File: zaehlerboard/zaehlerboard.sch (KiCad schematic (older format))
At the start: 10 parts, among them Q1 Q_Photo_NPN, U1 ESP1, U2 MCP1700-3.3, U3 LM293

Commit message: pin associations
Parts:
- C1: footprint Capacitor_THT:CP_Radial_D8.0mm_P5.00mm -> Capacitor_THT:C_Disc_D5.0mm_W2.5mm_P5.00mm
- R1, R2, R3: footprint (none) -> Resistor_THT:R_Axial_DIN0204_L3.6mm_D1.6mm_P7.62mm_Horizontal
- RV1: footprint (none) -> Potentiometer_THT:Potentiometer_ACP_CA9-V10_Vertical
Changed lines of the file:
@@
 F 0 "R2" H 5820 3396 50  0000 L CNN
 F 1 "22k" H 5820 3305 50  0000 L CNN
-F 2 "" V 5680 3350 50  0001 C CNN
+F 2 "Resistor_THT:R_Axial_DIN0204_L3.6mm_D1.6mm_P7.62mm_Horizontal" V 5680 3350 50  0001 C CNN
 F 3 "~" H 5750 3350 50  0001 C CNN
 	1    5750 3350
@@
 F 0 "R1" H 4630 3304 50  0000 R CNN
 F 1 "43" H 4630 3395 50  0000 R CNN
-F 2 "" V 4630 3350 50  0001 C CNN
+F 2 "Resistor_THT:R_Axial_DIN0204_L3.6mm_D1.6mm_P7.62mm_Horizontal" V 4630 3350 50  0001 C CNN
 F 3 "~" H 4700 3350 50  0001 C CNN
 	1    4700 3350
@@
 F 0 "RV1" V 6793 2550 50  0000 C CNN
 F 1 "10k" V 6884 2550 50  0000 C CNN
-F 2 "" H 7000 2550 50  0001 C CNN
+F 2 "Potentiometer_THT:Potentiometer_ACP_CA9-V10_Vertical" H 7000 2550 50  0001 C CNN
 F 3 "~" H 7000 2550 50  0001 C CNN
 	1    7000 2550
@@
 F 0 "C1" H 8465 3296 50  0000 L CNN
 F 1 "100nF" H 8465 3205 50  0000 L CNN
-F 2 "Capacitor_THT:CP_Radial_D8.0mm_P5.00mm" H 8388 3100 50  0001 C CNN
+F 2 "Capacitor_THT:C_Disc_D5.0mm_W2.5mm_P5.00mm" H 8388 3100 50  0001 C CNN
 F 3 "~" H 8350 3250 50  0001 C CNN
 	1    8350 3250
@@
 F 0 "R3" V 9843 1150 50  0000 C CNN
 F 1 "3k3" V 9934 1150 50  0000 C CNN
-F 2 "" V 9980 1150 50  0001 C CNN
+F 2 "Resistor_THT:R_Axial_DIN0204_L3.6mm_D1.6mm_P7.62mm_Horizontal" V 9980 1150 50  0001 C CNN
 F 3 "~" H 10050 1150 50  0001 C CNN
 	1    10050 1150

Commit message: update circuit
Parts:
- added J1: Screw_Terminal_01x02, TerminalBlock:TerminalBlock_Altech_AK300-2_P5.00mm, symbol Connector:Screw_Terminal_01x02
- RV1: footprint Potentiometer_THT:Potentiometer_ACP_CA9-V10_Vertical -> Potentiometer_THT:Potentiometer_ACP_CA9-H5_Horizontal
- U3: footprint Package_DIP:DIP-8_W10.16mm -> Package_DIP:DIP-8_W7.62mm_Socket
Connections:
- net GND: now also J1.1 (Pin_1)
- net VCC: now also J1.2 (Pin_2)
- net VDD: now also D1.2 (A); no longer D1.1 (K)
- net at R1.2: now also D1.1 (K); no longer D1.2 (A)
- no-connect marks 1 -> 0
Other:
- moved on the sheet: D1, U2, U3C
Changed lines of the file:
@@
 F 3 "~" H 4700 2650 50  0001 C CNN
 	1    4700 2650
-	0    1    1    0
+	0    -1   -1   0
 $EndComp
 $Comp
@@
 F 0 "U3" H 7450 2683 50  0000 C CNN
 F 1 "LM293" H 7450 2774 50  0000 C CNN
-F 2 "Package_DIP:DIP-8_W10.16mm" H 7400 3150 50  0001 C CNN
+F 2 "Package_DIP:DIP-8_W7.62mm_Socket" H 7400 3150 50  0001 C CNN
 F 3 "http://www.ti.com/lit/ds/symlink/tl081.pdf" H 7500 3250 50  0001 C CNN
 	1    7450 3050
@@
 	1    0    0    -1
 $EndComp
-$Comp
-L power:GND #PWR0105
-U 1 1 5D3768AA
-P 7650 2550
-F 0 "#PWR0105" H 7650 2300 50  0001 C CNN
-F 1 "GND" V 7655 2422 50  0000 R CNN
-F 2 "" H 7650 2550 50  0001 C CNN
-F 3 "" H 7650 2550 50  0001 C CNN
-	1    7650 2550
-	0    -1   -1   0
-$EndComp
 Wire Wire Line
 	6450 2550 6450 2400
@@
 L Regulator_Linear:MCP1700-3302E_TO92 U2
 U 1 1 5D3977D9
-P 3700 2050
-F 0 "U2" H 3700 1800 50  0000 C CNN
-F 1 "MCP1700-3.3" H 3700 1900 50  0000 C CNN
-F 2 "Package_TO_SOT_THT:TO-92" H 3700 2300 50  0001 C CIN
-F 3 "http://www.ti.com/lit/ds/symlink/lm1085.pdf" H 3700 2050 50  0001 C CNN
-	1    3700 2050
+P 3500 2500
+F 0 "U2" H 3500 2250 50  0000 C CNN
+F 1 "MCP1700-3.3" H 3500 2350 50  0000 C CNN
+F 2 "Package_TO_SOT_THT:TO-92" H 3500 2750 50  0001 C CIN
+F 3 "http://www.ti.com/lit/ds/symlink/lm1085.pdf" H 3500 2500 50  0001 C CNN
+	1    3500 2500
 	-1   0    0    1
 $EndComp
@@
 L power:GND #PWR02
 U 1 1 5D39ABD9
-P 3700 2900
-F 0 "#PWR02" H 3700 2650 50  0001 C CNN
-F 1 "GND" H 3705 2727 50  0000 C CNN
-F 2 "" H 3700 2900 50  0001 C CNN
-F 3 "" H 3700 2900 50  0001 C CNN
-	1    3700 2900
+P 3500 3350
+F 0 "#PWR02" H 3500 3100 50  0001 C CNN
+F 1 "GND" H 3505 3177 50  0000 C CNN
+F 2 "" H 3500 3350 50  0001 C CNN
+F 3 "" H 3500 3350 50  0001 C CNN
+	1    3500 3350
 	1    0    0    -1
 $EndComp
@@
 L power:VDD #PWR03
 U 1 1 5D39B7A3
-P 3250 1950
-F 0 "#PWR03" H 3250 1800 50  0001 C CNN
-F 1 "VDD" H 3267 2123 50  0000 C CNN
-F 2 "" H 3250 1950 50  0001 C CNN
-F 3 "" H 3250 1950 50  0001 C CNN
-	1    3250 1950
+P 3050 2400
+F 0 "#PWR03" H 3050 2250 50  0001 C CNN
+F 1 "VDD" H 3067 2573 50  0000 C CNN
+F 2 "" H 3050 2400 50  0001 C CNN
+F 3 "" H 3050 2400 50  0001 C CNN
+	1    3050 2400
 	1    0    0    -1
 $EndComp
@@
 L power:VCC #PWR01
 U 1 1 5D39C377
-P 4200 1950
-F 0 "#PWR01" H 4200 1800 50  0001 C CNN
-F 1 "VCC" H 4217 2123 50  0000 C CNN
-F 2 "" H 4200 1950 50  0001 C CNN
-F 3 "" H 4200 1950 50  0001 C CNN
-	1    4200 1950
+P 4000 2400
+F 0 "#PWR01" H 4000 2250 50  0001 C CNN
+F 1 "VCC" H 4017 2573 50  0000 C CNN
+F 2 "" H 4000 2400 50  0001 C CNN
+F 3 "" H 4000 2400 50  0001 C CNN
+	1    4000 2400
 	1    0    0    -1
 $EndComp
@@
 F 0 "RV1" V 6793 2550 50  0000 C CNN
 F 1 "10k" V 6884 2550 50  0000 C CNN
-F 2 "Potentiometer_THT:Potentiometer_ACP_CA9-V10_Vertical" H 7000 2550 50  0001 C CNN
+F 2 "Potentiometer_THT:Potentiometer_ACP_CA9-H5_Horizontal" H 7000 2550 50  0001 C CNN
 F 3 "~" H 7000 2550 50  0001 C CNN
 	1    7000 2550
@@
 Wire Wire Line
 	7000 2700 7000 2950
-NoConn ~ 7750 3650
-Wire Wire Line
-	7150 2550 7650 2550
+Wire Wire Line
+	7150 2550 7200 2550
 $Comp
 L Amplifier_Operational:LM2904 U3
 U 3 1 5D890418
-P 10150 2700
-F 0 "U3" H 10108 2746 50  0000 L CNN
-F 1 "LM293" H 10108 2655 50  0000 L CNN
-F 2 "Package_DIP:DIP-8_W10.16mm" H 10150 2700 50  0001 C CNN
-F 3 "http://www.ti.com/lit/ds/symlink/tl081.pdf" H 10150 2700 50  0001 C CNN
-	3    10150 2700
+P 7700 3050
+F 0 "U3" H 7658 3096 50  0000 L CNN
+F 1 "LM293" H 7658 3005 50  0000 L CNN
+F 2 "Package_DIP:DIP-8_W7.62mm_Socket" H 7700 3050 50  0001 C CNN
+F 3 "http://www.ti.com/lit/ds/symlink/tl081.pdf" H 7700 3050 50  0001 C CNN
+	3    7700 3050
 	1    0    0    -1
 $EndComp
@@
 L power:VDD #PWR04
 U 1 1 5D893A2A
-P 10050 2200
-F 0 "#PWR04" H 10050 2050 50  0001 C CNN
-F 1 "VDD" H 10067 2373 50  0000 C CNN
-F 2 "" H 10050 2200 50  0001 C CNN
-F 3 "" H 10050 2200 50  0001 C CNN
-	1    10050 2200
+P 7600 2750
+F 0 "#PWR04" H 7600 2600 50  0001 C CNN
+F 1 "VDD" H 7617 2923 50  0000 C CNN
+F 2 "" H 7600 2750 50  0001 C CNN
+F 3 "" H 7600 2750 50  0001 C CNN
+	1    7600 2750
 	1    0    0    -1
 $EndComp
@@
 L power:GND #PWR05
 U 1 1 5D894387
-P 10050 3150
-F 0 "#PWR05" H 10050 2900 50  0001 C CNN
-F 1 "GND" H 10055 2977 50  0000 C CNN
-F 2 "" H 10050 3150 50  0001 C CNN
-F 3 "" H 10050 3150 50  0001 C CNN
-	1    10050 3150
-	1    0    0    -1
-$EndComp
-Wire Wire Line
-	10050 2400 10050 2200
-Wire Wire Line
-	10050 3150 10050 3000
+P 7600 3350
+F 0 "#PWR05" H 7600 3100 50  0001 C CNN
+F 1 "GND" H 7605 3177 50  0000 C CNN
+F 2 "" H 7600 3350 50  0001 C CNN
+F 3 "" H 7600 3350 50  0001 C CNN
+	1    7600 3350
+	1    0    0    -1
+$EndComp
 $Comp
 L Device:C C1
@@
 F 3 "~" H 8350 3250 50  0001 C CNN
 	1    8350 3250
-	1    0    0    -1
-$EndComp
-$Comp
-L power:GND #PWR07
-U 1 1 5D89E950
-P 8350 3700
-F 0 "#PWR07" H 8350 3450 50  0001 C CNN
-F 1 "GND" H 8355 3527 50  0000 C CNN
-F 2 "" H 8350 3700 50  0001 C CNN
-F 3 "" H 8350 3700 50  0001 C CNN
-	1    8350 3700
 	1    0    0    -1
 $EndComp
@@
 	8350 3050 8350 3100
 Wire Wire Line
-	8350 3400 8350 3700
-Wire Wire Line
 	8350 3050 8350 1700
 Wire Wire Line
@@
 	9450 1050 9650 1050
 Wire Wire Line
-	3250 1950 3250 2050
-Wire Wire Line
-	3250 2050 3400 2050
-Wire Wire Line
-	4200 1950 4200 2050
-Wire Wire Line
-	4200 2050 4000 2050
-Wire Wire Line
-	3700 2350 3700 2900
+	3050 2400 3050 2500
+Wire Wire Line
+	3050 2500 3200 2500
+Wire Wire Line
+	4000 2400 4000 2500
+Wire Wire Line
+	4000 2500 3800 2500
+Wire Wire Line
+	3500 2800 3500 3350
+$Comp
+L Connector:Screw_Terminal_01x02 J1
+U 1 1 5D8B0312
+P 2500 2950
+F 0 "J1" H 2418 2717 50  0000 C CNN
+F 1 "Screw_Terminal_01x02" H 2418 2716 50  0001 C CNN
+F 2 "TerminalBlock:TerminalBlock_Altech_AK300-2_P5.00mm" H 2500 2950 50  0001 C CNN
+F 3 "~" H 2500 2950 50  0001 C CNN
+	1    2500 2950
+	-1   0    0    1
+$EndComp
+$Comp
+L power:GND #PWR0105
+U 1 1 5D3768AA
+P 7200 2650
+F 0 "#PWR0105" H 7200 2400 50  0001 C CNN
+F 1 "GND" V 7205 2522 50  0000 R CNN
+F 2 "" H 7200 2650 50  0001 C CNN
+F 3 "" H 7200 2650 50  0001 C CNN
+	1    7200 2650
+	1    0    0    -1
+$EndComp
+Wire Wire Line
+	7200 2650 7200 2550
+$Comp
+L power:VCC #PWR0106
+U 1 1 5D8F6DB0
+P 2700 2850
+F 0 "#PWR0106" H 2700 2700 50  0001 C CNN
+F 1 "VCC" H 2717 3023 50  0000 C CNN
+F 2 "" H 2700 2850 50  0001 C CNN
+F 3 "" H 2700 2850 50  0001 C CNN
+	1    2700 2850
+	1    0    0    -1
+$EndComp
+$Comp
+L power:GND #PWR0108
+U 1 1 5D8F783F
+P 2700 2950
+F 0 "#PWR0108" H 2700 2700 50  0001 C CNN
+F 1 "GND" H 2705 2777 50  0000 C CNN
+F 2 "" H 2700 2950 50  0001 C CNN
+F 3 "" H 2700 2950 50  0001 C CNN
+	1    2700 2950
+	1    0    0    -1
+$EndComp
+$Comp
+L power:GND #PWR07
+U 1 1 5D89E950
+P 8350 3800
+F 0 "#PWR07" H 8350 3550 50  0001 C CNN
+F 1 "GND" H 8355 3627 50  0000 C CNN
+F 2 "" H 8350 3800 50  0001 C CNN
+F 3 "" H 8350 3800 50  0001 C CNN
+	1    8350 3800
+	1    0    0    -1
+$EndComp
+Wire Wire Line
+	8350 3400 8350 3800
 $EndSCHEMATC

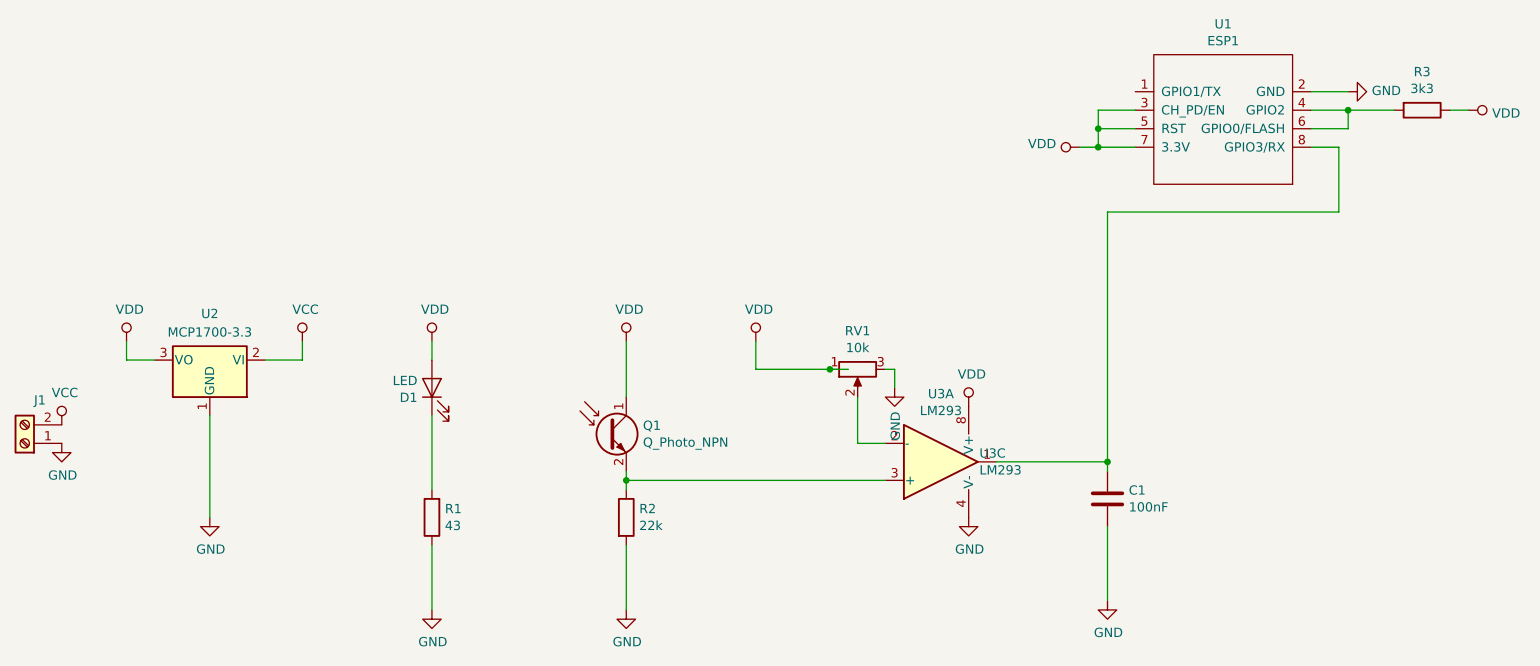
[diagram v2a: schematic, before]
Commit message: additional elements and new board layout
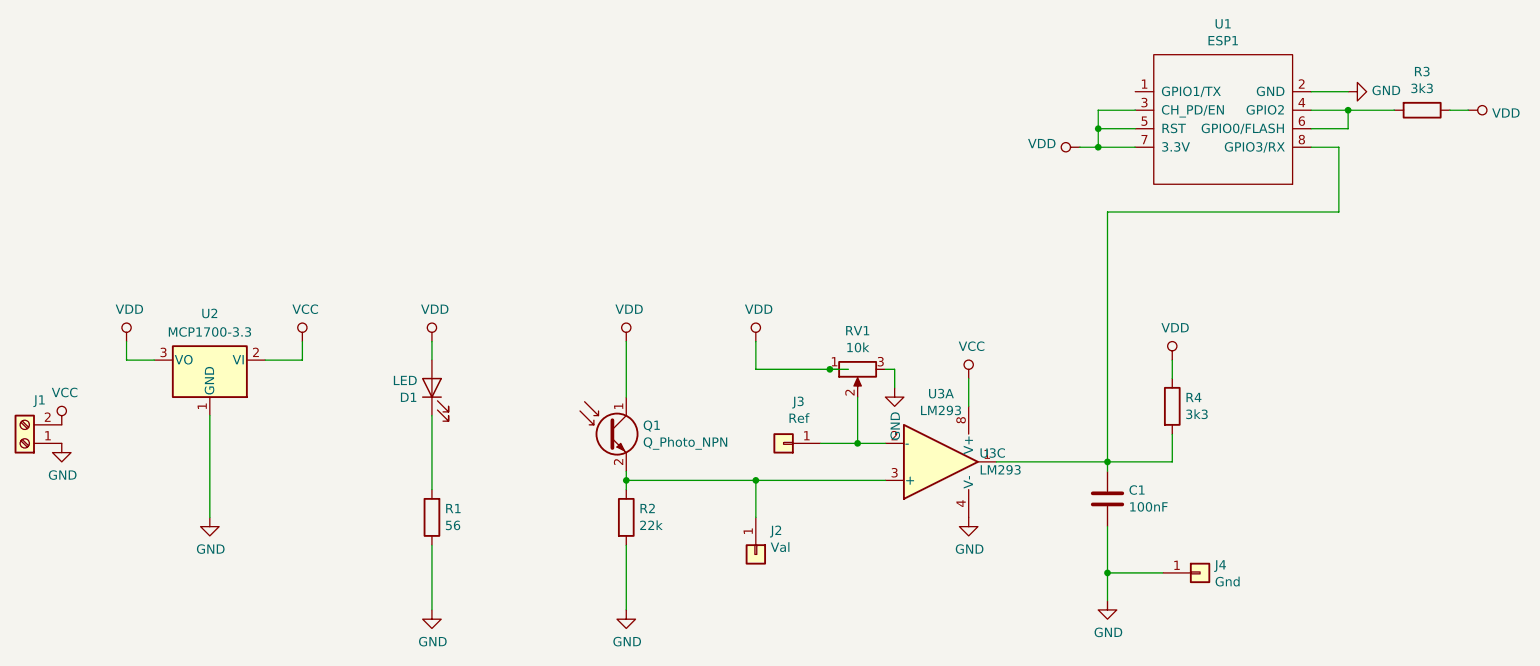
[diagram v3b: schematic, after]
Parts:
- added J2: Val, Connector_Pin:Pin_D0.7mm_L6.5mm_W1.8mm_FlatFork, symbol Connector_Generic:Conn_01x01
- added J3: Ref, Connector_Pin:Pin_D0.7mm_L6.5mm_W1.8mm_FlatFork, symbol Connector_Generic:Conn_01x01
- added J4: Gnd, Connector_Pin:Pin_D0.7mm_L6.5mm_W1.8mm_FlatFork, symbol Connector_Generic:Conn_01x01
- added R4: 3k3, Resistor_THT:R_Axial_DIN0204_L3.6mm_D1.6mm_P7.62mm_Horizontal, symbol Device:R
- R1: value 43 -> 56
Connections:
- net GND: now also J4.1 (Pin_1)
- net VCC: now also U3.8 (V+)
- net VDD: now also R4.1; no longer U3.8 (V+)
- net at Q1.2 (E), R2.1, U3.3 (+): now also J2.1 (Pin_1)
- net at C1.1, U1.8 (GPIO3/RX), U3.1: now also R4.2
- net at RV1.2, U3.2 (-): now also J3.1 (Pin_1)
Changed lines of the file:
@@
 P 4700 3350
 F 0 "R1" H 4630 3304 50  0000 R CNN
-F 1 "43" H 4630 3395 50  0000 R CNN
+F 1 "56" H 4630 3395 50  0000 R CNN
 F 2 "Resistor_THT:R_Axial_DIN0204_L3.6mm_D1.6mm_P7.62mm_Horizontal" V 4630 3350 50  0001 C CNN
 F 3 "~" H 4700 3350 50  0001 C CNN
@@
 	5750 3100 5750 3150
 Wire Wire Line
-	7150 3150 5750 3150
+	7150 3150 6450 3150
 Connection ~ 5750 3150
 Wire Wire Line
@@
 	6850 2550 6950 2550
 Wire Wire Line
-	7000 2700 7000 2950
-Wire Wire Line
 	7150 2550 7200 2550
 $Comp
@@
 F 3 "http://www.ti.com/lit/ds/symlink/tl081.pdf" H 7700 3050 50  0001 C CNN
 	3    7700 3050
-	1    0    0    -1
-$EndComp
-$Comp
-L power:VDD #PWR04
-U 1 1 5D893A2A
-P 7600 2750
-F 0 "#PWR04" H 7600 2600 50  0001 C CNN
-F 1 "VDD" H 7617 2923 50  0000 C CNN
-F 2 "" H 7600 2750 50  0001 C CNN
-F 3 "" H 7600 2750 50  0001 C CNN
-	1    7600 2750
 	1    0    0    -1
 $EndComp
@@
 $EndComp
 Wire Wire Line
-	8350 3400 8350 3800
+	8350 3400 8350 3650
+$Comp
+L power:VCC #PWR04
+U 1 1 5D970631
+P 7600 2600
+F 0 "#PWR04" H 7600 2450 50  0001 C CNN
+F 1 "VCC" H 7617 2773 50  0000 C CNN
+F 2 "" H 7600 2600 50  0001 C CNN
+F 3 "" H 7600 2600 50  0001 C CNN
+	1    7600 2600
+	1    0    0    -1
+$EndComp
+Wire Wire Line
+	7600 2600 7600 2750
+$Comp
+L Device:R R4
+U 1 1 5D971A9F
+P 8700 2750
+F 0 "R4" H 8770 2796 50  0000 L CNN
+F 1 "3k3" H 8770 2705 50  0000 L CNN
+F 2 "Resistor_THT:R_Axial_DIN0204_L3.6mm_D1.6mm_P7.62mm_Horizontal" V 8630 2750 50  0001 C CNN
+F 3 "~" H 8700 2750 50  0001 C CNN
+	1    8700 2750
+	1    0    0    -1
+$EndComp
+$Comp
+L power:VDD #PWR010
+U 1 1 5D972537
+P 8700 2500
+F 0 "#PWR010" H 8700 2350 50  0001 C CNN
+F 1 "VDD" H 8717 2673 50  0000 C CNN
+F 2 "" H 8700 2500 50  0001 C CNN
+F 3 "" H 8700 2500 50  0001 C CNN
+	1    8700 2500
+	1    0    0    -1
+$EndComp
+Wire Wire Line
+	8700 2500 8700 2600
+Wire Wire Line
+	8700 2900 8700 3050
+Wire Wire Line
+	8700 3050 8350 3050
+$Comp
+L Connector_Generic:Conn_01x01 J3
+U 1 1 5D978361
+P 6600 2950
+F 0 "J3" H 6518 2725 50  0000 C CNN
+F 1 "Ref" H 6518 2816 50  0000 C CNN
+F 2 "Connector_Pin:Pin_D0.7mm_L6.5mm_W1.8mm_FlatFork" H 6600 2950 50  0001 C CNN
+F 3 "~" H 6600 2950 50  0001 C CNN
+	1    6600 2950
+	-1   0    0    1
+$EndComp
+Connection ~ 7000 2950
+$Comp
+L Connector_Generic:Conn_01x01 J2
+U 1 1 5D979C69
+P 6450 3550
+F 0 "J2" V 6322 3630 50  0000 L CNN
+F 1 "Val" V 6413 3630 50  0000 L CNN
+F 2 "Connector_Pin:Pin_D0.7mm_L6.5mm_W1.8mm_FlatFork" H 6450 3550 50  0001 C CNN
+F 3 "~" H 6450 3550 50  0001 C CNN
+	1    6450 3550
+	0    1    1    0
+$EndComp
+Wire Wire Line
+	6450 3350 6450 3150
+Connection ~ 6450 3150
+Wire Wire Line
+	6450 3150 5750 3150
+$Comp
+L Connector_Generic:Conn_01x01 J4
+U 1 1 5D97B40C
+P 8850 3650
+F 0 "J4" H 8930 3692 50  0000 L CNN
+F 1 "Gnd" H 8930 3601 50  0000 L CNN
+F 2 "Connector_Pin:Pin_D0.7mm_L6.5mm_W1.8mm_FlatFork" H 8850 3650 50  0001 C CNN
+F 3 "~" H 8850 3650 50  0001 C CNN
+	1    8850 3650
+	1    0    0    -1
+$EndComp
+Wire Wire Line
+	8650 3650 8350 3650
+Connection ~ 8350 3650
+Wire Wire Line
+	8350 3650 8350 3800
+Wire Wire Line
+	6800 2950 7000 2950
+Wire Wire Line
+	7000 2700 7000 2950
 $EndSCHEMATC
